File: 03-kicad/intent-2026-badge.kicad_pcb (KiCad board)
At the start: 2 copper layers, 56 x 125.5 mm, 95 parts, among them J1 TYPE-C-31-M-12, J2 HACK HEADER, J3 BATT 3xAAA, J5 SAO1 IR, J6 SAO2 IMU, J7 SAO3 SPK, J8 OLED 0.96 I2C, P1 IR MODULE, P2 IMU MODULE, P3 SPK MODULE, Q1 HL3401, Q2 S8050, SW1 BOOTSEL, SW2 A, SW3 B, SW4 C, SW6 RESET, U1 RP2040, U2 W25Q16JVSNIQ, U3 AP2112K-3.3TRG1, U4 USBLC6-2SC6, U5 IRM-H638T/TR2, U6 SN74LV1T34DBVR, U7 LSM6DS3TR-C, Y1 12MHz ABM8-272-T3

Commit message: Speaker can gets a horizontal label band; module back texts back to the original orientation
Co-Authored-By: Claude Opus 5.5 (1M context) <noreply@anthropic.com>
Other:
- board text added: "B3 · BEEP FIZZ"
- board text removed: "B3"
- board text removed: "BEEP FIZZ"
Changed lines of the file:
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@@
 		(layer "F.SilkS")
 	)
+	(gr_line
+		(start 138.2 167.4)
+		(end 149.8 167.4)
+		(stroke
+			(width 0.15)
+			(type default)
+		)
+		(layer "F.SilkS")
+	)
+	(gr_line
+		(start 138.2 169.1)
+		(end 149.8 169.1)
+		(stroke
+			(width 0.15)
+			(type default)
+		)
+		(layer "F.SilkS")
+	)
 	(gr_arc
 		(start 139.2 90)
@@
 		)
 	)
-	(gr_text "38k"
-		(at 117.5 169.5 270)
+	(gr_text "B3 · BEEP FIZZ"
+		(at 144 168.25 180)
 		(layer "F.SilkS")
 		(effects
@@
 		)
 	)
-	(gr_text "BEEP FIZZ"
-		(at 138.45 170.6 270)
-		(layer "F.SilkS")
-		(effects
-			(font
-				(size 0.8 0.8)
-				(thickness 0.15)
-			)
-		)
-	)
-	(gr_text "B3"
-		(at 149.65 170.6 270)
+	(gr_text "38k"
+		(at 117.5 169.5 270)
 		(layer "F.SilkS")
 		(effects
@@
 		)
 	)
-	(gr_text "AUTHORIZED PERSONNEL ONLY"
-		(at 128 79.4 0)
+	(gr_text "B1 IR MODULE"
+		(at 112 155.6 0)
 		(layer "B.SilkS")
 		(effects
@@
 		)
 	)
-	(gr_text "MODEL VM-2026 · 3V3 · 2 LAYERS"
-		(at 128 81 0)
+	(gr_text "snap off,"
+		(at 112 157.4 0)
 		(layer "B.SilkS")
 		(effects
@@
 		)
 	)
-	(gr_text "NO USER-SERVICEABLE PARTS INSIDE (JK, SEE J2)"
-		(at 128 82.6 0)
+	(gr_text "plug into J5"
+		(at 112 159.000001 0)
 		(layer "B.SilkS")
 		(effects
@@
 		)
 	)
-	(gr_text "SW5: optional (DNP)"
-		(at 137.5 137.5 0)
+	(gr_text "AUTHORIZED PERSONNEL ONLY"
+		(at 128 79.4 0)
 		(layer "B.SilkS")
 		(effects
@@
 		)
 	)
-	(gr_text "JP1: cut for SW5"
-		(at 137.5 139.3 0)
+	(gr_text "MODEL VM-2026 · 3V3 · 2 LAYERS"
+		(at 128 81 0)
 		(layer "B.SilkS")
 		(effects
@@
 		)
 	)
-	(gr_text "3V3 INSIDE"
-		(at 151.2 92.1 0)
+	(gr_text "NO USER-SERVICEABLE PARTS INSIDE (JK, SEE J2)"
+		(at 128 82.6 0)
 		(layer "B.SilkS")
 		(effects
@@
 		)
 	)
-	(gr_text "plug into J5"
-		(at 112 155.599999 180)
+	(gr_text "B2 IMU MODULE"
+		(at 128 155.6 0)
 		(layer "B.SilkS")
 		(effects
@@
 	)
 	(gr_text "snap off,"
-		(at 112 157.2 180)
+		(at 128 157.4 0)
 		(layer "B.SilkS")
 		(effects
@@
 		)
 	)
-	(gr_text "B1 IR MODULE"
-		(at 112 159 180)
+	(gr_text "plug into J6"
+		(at 128 159.000001 0)
 		(layer "B.SilkS")
 		(effects
@@
 		)
 	)
-	(gr_text "plug into J6"
-		(at 128 155.599999 180)
+	(gr_text "SW5: optional (DNP)"
+		(at 137.5 137.5 0)
 		(layer "B.SilkS")
 		(effects
@@
 		)
 	)
-	(gr_text "snap off,"
-		(at 128 157.2 180)
+	(gr_text "JP1: cut for SW5"
+		(at 137.5 139.3 0)
 		(layer "B.SilkS")
 		(effects
@@
 		)
 	)
-	(gr_text "B2 IMU MODULE"
-		(at 128 159 180)
+	(gr_text "B3 SPK MODULE"
+		(at 144 155.6 0)
 		(layer "B.SilkS")
 		(effects
@@
 		)
 	)
-	(gr_text "plug into J7"
-		(at 144 155.599999 180)
+	(gr_text "snap off,"
+		(at 144 157.4 0)
 		(layer "B.SilkS")
 		(effects
@@
 		)
 	)
-	(gr_text "snap off,"
-		(at 144 157.2 180)
+	(gr_text "plug into J7"
+		(at 144 159.000001 0)
 		(layer "B.SilkS")
 		(effects
@@
 		)
 	)
-	(gr_text "B3 SPK MODULE"
-		(at 144 159 180)
+	(gr_text "3V3 INSIDE"
+		(at 151.2 92.1 0)
 		(layer "B.SilkS")
 		(effects

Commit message: Module back texts turned 180 deg again; stale SW5/JP1/J3 back-silk notes removed
Co-Authored-By: Claude Opus 5.5 (1M context) <noreply@anthropic.com>
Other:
- board text added: "OLED Display"
- board text removed: "JP1: cut for SW5"
- board text removed: "SW5: optional (DNP)"
- board text removed: "battery lead → J3 (front, bottom)"
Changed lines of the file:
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@@
+		)
+	)
+	(gr_text "OLED Display"
+		(at 109.26 76.5 0)
+		(layer "F.SilkS")
+		(effects
+			(font
+				(size 1 1)
+				(thickness 0.15)
+			)
+			(justify left bottom)
 		)
 	)
@@
 		)
 	)
-	(gr_text "B1 IR MODULE"
-		(at 112 155.6 0)
-		(layer "B.SilkS")
-		(effects
-			(font
-				(size 0.8 0.8)
-				(thickness 0.15)
-			)
-			(justify mirror)
-		)
-	)
-	(gr_text "snap off,"
-		(at 112 157.4 0)
-		(layer "B.SilkS")
-		(effects
-			(font
-				(size 0.8 0.8)
-				(thickness 0.15)
-			)
-			(justify mirror)
-		)
-	)
-	(gr_text "plug into J5"
-		(at 112 159.000001 0)
-		(layer "B.SilkS")
-		(effects
-			(font
-				(size 0.8 0.8)
-				(thickness 0.15)
-			)
-			(justify mirror)
-		)
-	)
 	(gr_text "AUTHORIZED PERSONNEL ONLY"
 		(at 128 79.4 0)
@@
 		)
 	)
-	(gr_text "B2 IMU MODULE"
-		(at 128 155.6 0)
-		(layer "B.SilkS")
-		(effects
-			(font
-				(size 0.8 0.8)
-				(thickness 0.15)
-			)
-			(justify mirror)
-		)
-	)
-	(gr_text "snap off,"
-		(at 128 157.4 0)
-		(layer "B.SilkS")
-		(effects
-			(font
-				(size 0.8 0.8)
-				(thickness 0.15)
-			)
-			(justify mirror)
-		)
-	)
-	(gr_text "plug into J6"
-		(at 128 159.000001 0)
-		(layer "B.SilkS")
-		(effects
-			(font
-				(size 0.8 0.8)
-				(thickness 0.15)
-			)
-			(justify mirror)
-		)
-	)
-	(gr_text "SW5: optional (DNP)"
-		(at 137.5 137.5 0)
-		(layer "B.SilkS")
-		(effects
-			(font
-				(size 0.8 0.8)
-				(thickness 0.15)
-			)
-			(justify mirror)
-		)
-	)
-	(gr_text "JP1: cut for SW5"
-		(at 137.5 139.3 0)
-		(layer "B.SilkS")
-		(effects
-			(font
-				(size 0.8 0.8)
-				(thickness 0.15)
-			)
-			(justify mirror)
-		)
-	)
-	(gr_text "B3 SPK MODULE"
-		(at 144 155.6 0)
-		(layer "B.SilkS")
-		(effects
-			(font
-				(size 0.8 0.8)
-				(thickness 0.15)
-			)
-			(justify mirror)
-		)
-	)
-	(gr_text "snap off,"
-		(at 144 157.4 0)
-		(layer "B.SilkS")
-		(effects
-			(font
-				(size 0.8 0.8)
-				(thickness 0.15)
-			)
-			(justify mirror)
-		)
-	)
-	(gr_text "plug into J7"
-		(at 144 159.000001 0)
-		(layer "B.SilkS")
-		(effects
-			(font
-				(size 0.8 0.8)
-				(thickness 0.15)
-			)
-			(justify mirror)
-		)
-	)
 	(gr_text "3V3 INSIDE"
 		(at 151.2 92.1 0)
@@
 		)
 	)
+	(gr_text "plug into J5"
+		(at 112 155.599999 180)
+		(layer "B.SilkS")
+		(effects
+			(font
+				(size 0.8 0.8)
+				(thickness 0.15)
+			)
+			(justify mirror)
+		)
+	)
+	(gr_text "snap off,"
+		(at 112 157.2 180)
+		(layer "B.SilkS")
+		(effects
+			(font
+				(size 0.8 0.8)
+				(thickness 0.15)
+			)
+			(justify mirror)
+		)
+	)
+	(gr_text "B1 IR MODULE"
+		(at 112 159 180)
+		(layer "B.SilkS")
+		(effects
+			(font
+				(size 0.8 0.8)
+				(thickness 0.15)
+			)
+			(justify mirror)
+		)
+	)
+	(gr_text "plug into J6"
+		(at 128 155.599999 180)
+		(layer "B.SilkS")
+		(effects
+			(font
+				(size 0.8 0.8)
+				(thickness 0.15)
+			)
+			(justify mirror)
+		)
+	)
+	(gr_text "snap off,"
+		(at 128 157.2 180)
+		(layer "B.SilkS")
+		(effects
+			(font
+				(size 0.8 0.8)
+				(thickness 0.15)
+			)
+			(justify mirror)
+		)
+	)
+	(gr_text "B2 IMU MODULE"
+		(at 128 159 180)
+		(layer "B.SilkS")
+		(effects
+			(font
+				(size 0.8 0.8)
+				(thickness 0.15)
+			)
+			(justify mirror)
+		)
+	)
+	(gr_text "plug into J7"
+		(at 144 155.599999 180)
+		(layer "B.SilkS")
+		(effects
+			(font
+				(size 0.8 0.8)
+				(thickness 0.15)
+			)
+			(justify mirror)
+		)
+	)
+	(gr_text "snap off,"
+		(at 144 157.2 180)
+		(layer "B.SilkS")
+		(effects
+			(font
+				(size 0.8 0.8)
+				(thickness 0.15)
+			)
+			(justify mirror)
+		)
+	)
+	(gr_text "B3 SPK MODULE"
+		(at 144 159 180)
+		(layer "B.SilkS")
+		(effects
+			(font
+				(size 0.8 0.8)
+				(thickness 0.15)
+			)
+			(justify mirror)
+		)
+	)
 	(gr_text "3×AAA BATTERY BOX · tape here · switch on box"
 		(at 128 84.4 0)
@@
 		(layer "B.SilkS")
 		(effects
-			(font
-				(size 0.9 0.9)
-				(thickness 0.15)
-			)
-			(justify mirror)
-		)
-	)
-	(gr_text "battery lead → J3 (front, bottom)"
-		(at 115 136 0)
-		(layer "B.SilkS")
-		(effects

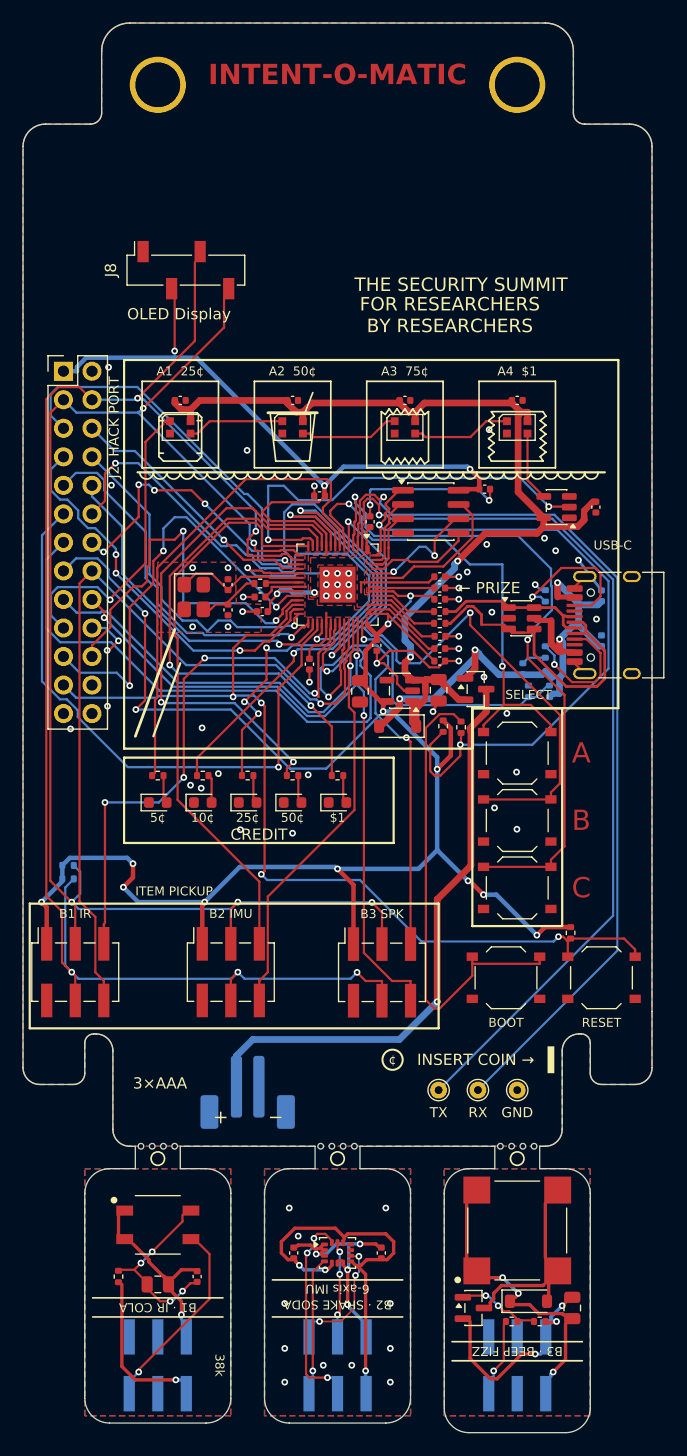
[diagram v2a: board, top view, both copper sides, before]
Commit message: Board: Benny's KiCad silk edits (IR can 38k text removed, tagline merged)
Co-Authored-By: Claude Opus 5.5 (1M context) <noreply@anthropic.com>
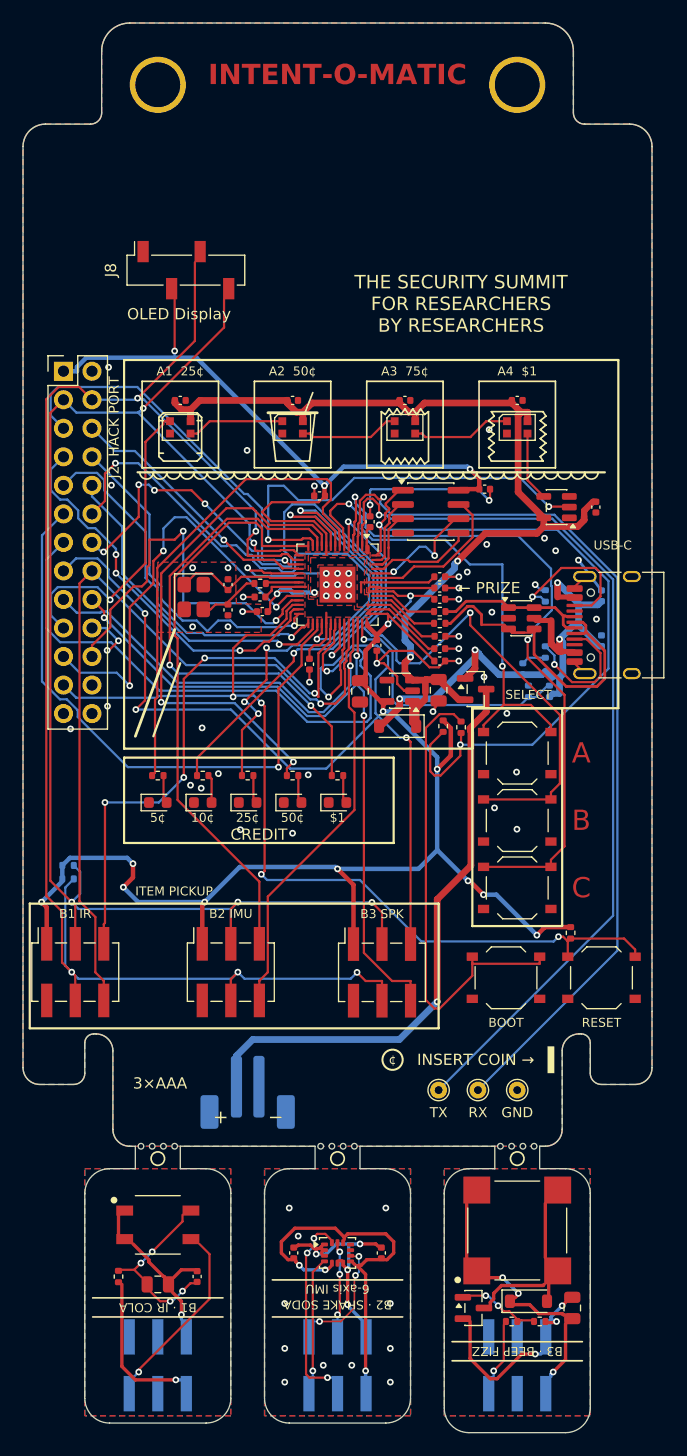
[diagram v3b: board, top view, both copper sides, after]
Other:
- board text added: "THE SECURITY SUMMIT FOR RESEARCHERS BY RESEARCHERS"
- board text removed: "38k"
- board text removed: "FOR RESEARCHERS BY RESEARCHERS"
- board text removed: "THE SECURITY SUMMIT"
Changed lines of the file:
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@@
-		)
-	)
-	(gr_text "38k"
-		(at 117.5 169.5 270)
-		(layer "F.SilkS")
-		(effects
-			(font
-				(size 0.8 0.8)
-				(thickness 0.15)
-			)
 		)
 	)
@@
 		)
 	)
-	(gr_text "FOR RESEARCHERS\nBY RESEARCHERS"
-		(at 138 76 0)
+	(gr_text "THE SECURITY SUMMIT\nFOR RESEARCHERS\nBY RESEARCHERS"
+		(at 139 75 0)
 		(layer "F.SilkS")
 		(effects
-			(font
-				(size 1.2 1.2)
-				(thickness 0.2)
-			)
-		)
-	)
-	(gr_text "THE SECURITY SUMMIT"
-		(at 139 73.3 0)
-		(layer "F.SilkS")
-		(effects
